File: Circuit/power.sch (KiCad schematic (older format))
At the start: 19 parts, among them Q202 FDN340P, Q203 FDN340P, SW1 ON/OFF, U201 CN3063, U202 MCP6002, U3 LXDC2XQ

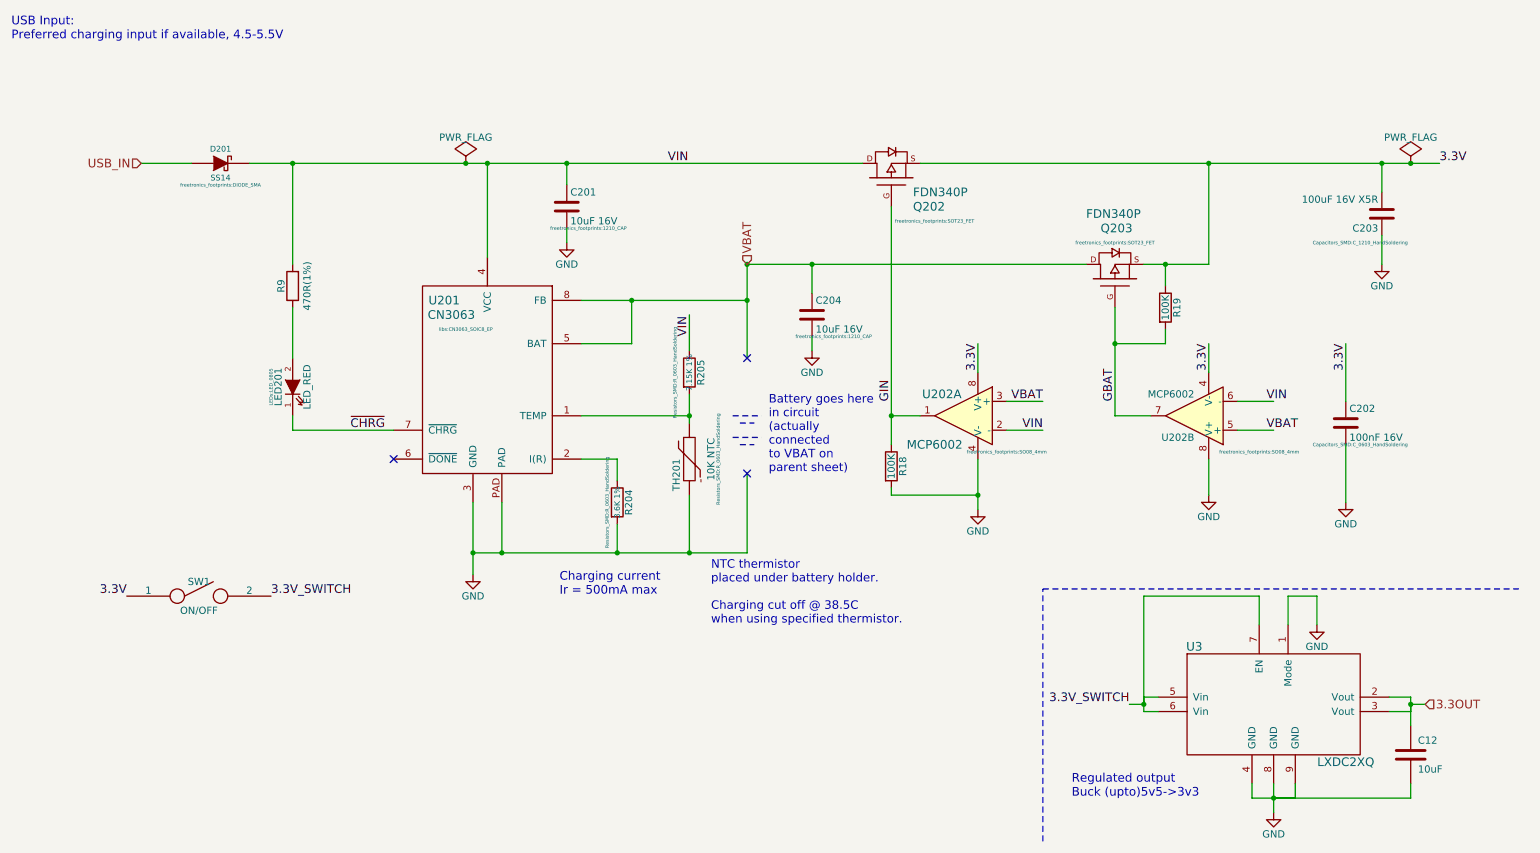
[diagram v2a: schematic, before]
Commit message: BOM information to schematic. Power & main sheets mostly.
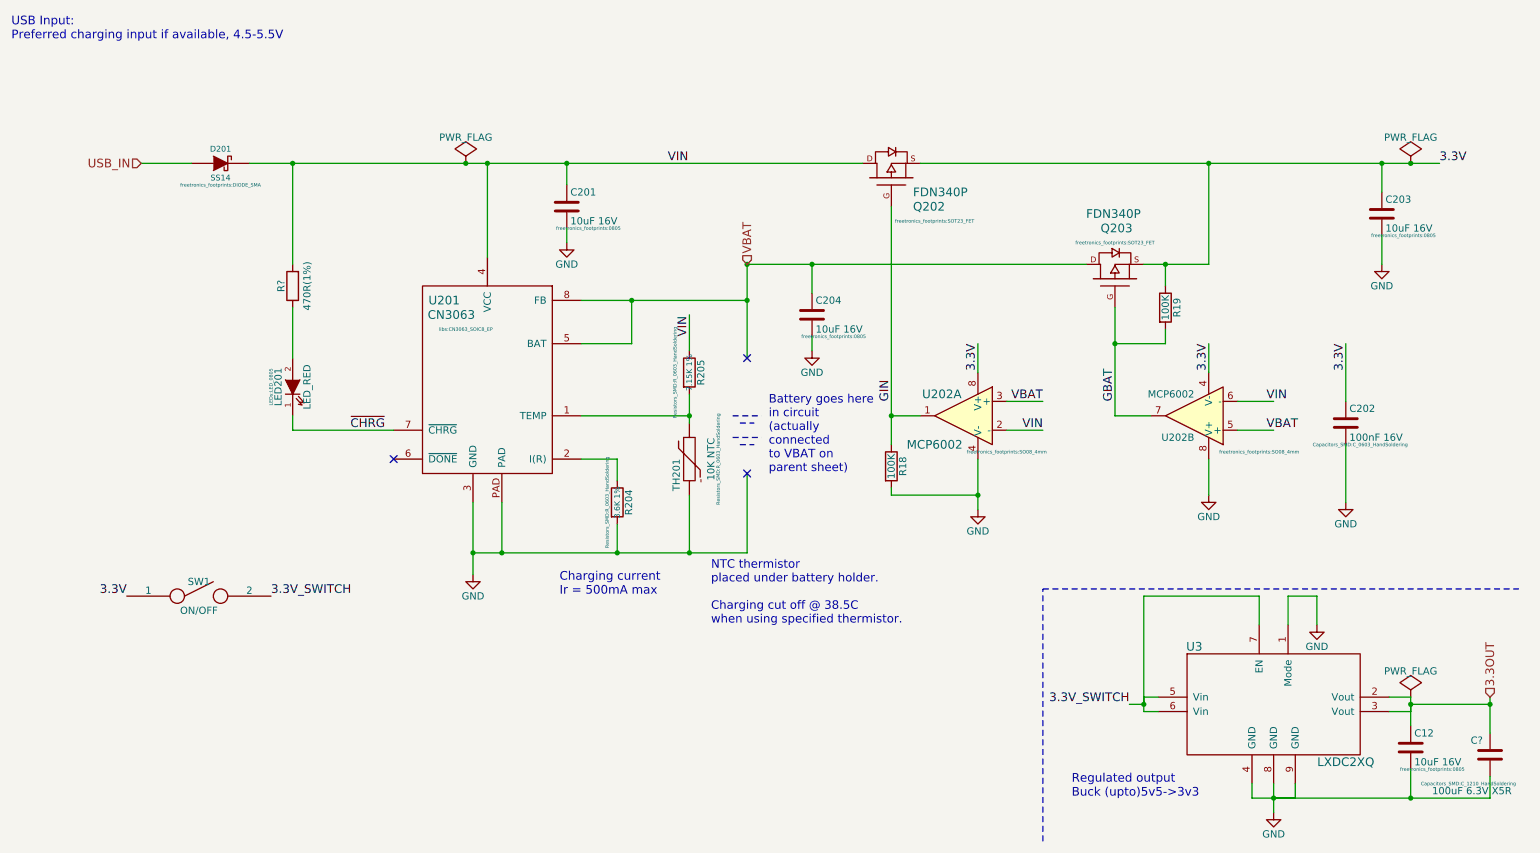
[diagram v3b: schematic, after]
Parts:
- removed C12: 10uF, Capacitors_SMD:C_0603_HandSoldering, symbol CAP
- added C12, C203: 10uF 16V, freetronics_footprints:0805, symbol C
- C201, C204: footprint freetronics_footprints:1210_CAP -> freetronics_footprints:0805; Digikey PN 1276-2865-1-ND -> 1276-2399-1-ND; Link http://www.digikey.com.au/product-detail/en/samsung-electro-mechanics-america-inc/CL32F106ZOHNNNE/1276-2865-1-ND/3890951 -> http://www.digikey.com.au/product-detail/en/samsung-electro-mechanics-america-inc/CL21A106KOCLRNC/1276-2399-1-ND/3890485; Manufacturer PN CL32F106ZOHNNNE -> CL21A106KOCLRNC; Unit Cost 0.29 -> 0.18
- C?: renamed from C203; value 100uF 16V X5R -> 100uF 6.3V X5R; Digikey PN (none) -> 490-7217-1-ND; Link (none) -> http://www.digikey.com.au/product-detail/en/murata-electron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; Manufacturer PN (none) -> GRM31CR60J107ME39K; Unit Cost (none) -> 0.60
- U202: Digikey PN (none) -> MCP6002T-I/SNCT-ND; Link (none) -> http://www.digikey.com.au/product-detail/en/microchip-techn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; Manufacturer PN (none) -> MCP6002T-I/SN; Unit Cost (none) -> 0.33
- renumbered R9 to R?
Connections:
- wire segments 72 -> 74
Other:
- moved on the sheet: C?
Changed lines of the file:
@@
 Text Label 6850 3450 1    60   ~ 0
 GIN
-Text HLabel 10550 5550 2    60   Input ~ 0
+Text HLabel 11000 5500 1    60   Input ~ 0
 3.3OUT
 $Comp
@@
 F 2 "freetronics_footprints:SO08_4mm" H 7050 3300 24  0000 C CNN
 F 3 "" H 7350 3550 60  0000 C CNN
+F 4 "MCP6002T-I/SNCT-ND" H 7350 3550 60  0001 C CNN "Digikey PN"
+F 5 "http://www.digikey.com.au/product-detail/en/microchip-technology/MCP6002T-I-SN/MCP6002T-I-SNCT-ND/4307905" H 7350 3550 60  0001 C CNN "Link"
+F 6 "MCP6002T-I/SN" H 7350 3550 60  0001 C CNN "Manufacturer PN"
+F 7 "0.33" H 7350 3550 60  0001 C CNN "Unit Cost"
 	1    7350 3550
 	-1   0    0    -1
@@
 VIN
 $Comp
-L C C203
+L C C?
 U 1 1 5642CCBE
-P 10250 2150
-F 0 "C203" H 10275 2250 50  0000 L CNN
-F 1 "100uF 16V X5R" H 10275 2050 50  0000 L CNN
-F 2 "Capacitors_SMD:C_1210_HandSoldering" H 10400 2350 24  0000 C CNN
-F 3 "" H 10250 2150 60  0000 C CNN
-	1    10250 2150
+P 11000 5900
+F 0 "C?" H 11050 5800 50  0000 L CNN
+F 1 "100uF 6.3V X5R" H 10850 6150 50  0000 L CNN
+F 2 "Capacitors_SMD:C_1210_HandSoldering" H 11150 6100 24  0000 C CNN
+F 3 "" H 11000 5900 60  0000 C CNN
+F 4 "490-7217-1-ND" H 11000 5900 60  0001 C CNN "Digikey PN"
+F 5 "http://www.digikey.com.au/product-detail/en/murata-electronics-north-america/GRM31CR60J107ME39K/490-7217-1-ND/3991203" H 11000 5900 60  0001 C CNN "Link"
+F 6 "GRM31CR60J107ME39K" H 11000 5900 60  0001 C CNN "Manufacturer PN"
+F 7 "0.60" H 11000 5900 60  0001 C CNN "Unit Cost"
+	1    11000 5900
 	-1   0    0    1
 $EndComp
@@
 F 0 "C201" H 4625 2200 50  0000 L CNN
 F 1 "10uF 16V" H 4625 2000 50  0000 L CNN
-F 2 "freetronics_footprints:1210_CAP" H 4750 1950 24  0000 C CNN
+F 2 "freetronics_footprints:0805" H 4750 1950 24  0000 C CNN
 F 3 "" H 4600 2100 60  0000 C CNN
-F 4 "1276-2865-1-ND" H 4600 2100 60  0001 C CNN "Digikey PN"
-F 5 "http://www.digikey.com.au/product-detail/en/samsung-electro-mechanics-america-inc/CL32F106ZOHNNNE/1276-2865-1-ND/3890951" H 4600 2100 60  0001 C CNN "Link"
-F 6 "CL32F106ZOHNNNE" H 4600 2100 60  0001 C CNN "Manufacturer PN"
-F 7 "0.29" H 4600 2100 60  0001 C CNN "Unit Cost"
+F 4 "1276-2399-1-ND" H 4600 2100 60  0001 C CNN "Digikey PN"
+F 5 "http://www.digikey.com.au/product-detail/en/samsung-electro-mechanics-america-inc/CL21A106KOCLRNC/1276-2399-1-ND/3890485" H 4600 2100 60  0001 C CNN "Link"
+F 6 "CL21A106KOCLRNC" H 4600 2100 60  0001 C CNN "Manufacturer PN"
+F 7 "0.18" H 4600 2100 60  0001 C CNN "Unit Cost"
 	1    4600 2100
 	1    0    0    -1
@@
 	1    0    0    -1
 $EndComp
-$Comp
-L CAP C12
-U 1 1 5812F47A
-P 10450 5900
-F 0 "C12" H 10500 6000 50  0000 L CNN
-F 1 "10uF" H 10500 5800 50  0000 L CNN
-F 2 "Capacitors_SMD:C_0603_HandSoldering" H 10450 5900 60  0001 C CNN
-F 3 "" H 10450 5900 60  0000 C CNN
-	1    10450 5900
-	1    0    0    -1
-$EndComp
 Wire Wire Line
 	5050 3050 5050 2750
@@
 	10450 5500 10450 5600
 Wire Wire Line
-	10450 5550 10550 5550
+	10450 5550 11000 5550
 Wire Wire Line
 	10450 5600 10300 5600
@@
 	10450 5550 10450 5700
 Wire Wire Line
-	10450 6100 10450 6200
-Wire Wire Line
-	10450 6200 9500 6200
+	10450 6000 10450 6200
+Wire Wire Line
+	9500 6200 11000 6200
 $Comp
 L LXDC2XQ U3
@@
 NoConn ~ 5850 3950
 $Comp
-L R R9
+L R R?
 U 1 1 5820F348
 P 2700 2650
-F 0 "R9" V 2780 2650 50  0000 C CNN
+F 0 "R?" V 2780 2650 50  0000 C CNN
 F 1 "470R(1%)" V 2600 2650 50  0000 C CNN
 F 2 "Resistors_SMD:R_0603_HandSoldering" V 2630 2650 50  0001 C CNN
@@
 	-1   0    0    1
 $EndComp
+Wire Wire Line
+	11000 5500 11000 5750
+Connection ~ 11000 5550
+Wire Wire Line
+	11000 6200 11000 6050
+Connection ~ 10450 6200
+$Comp
+L PWR_FLAG #FLG?
+U 1 1 58217320
+P 10450 5500
+F 0 "#FLG?" H 10450 5595 50  0001 C CNN
+F 1 "PWR_FLAG" H 10450 5680 50  0000 C CNN
+F 2 "" H 10450 5500 60  0000 C CNN
+F 3 "" H 10450 5500 60  0000 C CNN
+	1    10450 5500
+	1    0    0    -1
+$EndComp
 $Comp
 L C C204
-U 1 1 5820F69B
+U 1 1 58217FC8
 P 6300 2850
 F 0 "C204" H 6325 2950 50  0000 L CNN
 F 1 "10uF 16V" H 6325 2750 50  0000 L CNN
-F 2 "freetronics_footprints:1210_CAP" H 6450 2700 24  0000 C CNN
+F 2 "freetronics_footprints:0805" H 6450 2700 24  0000 C CNN
 F 3 "" H 6300 2850 60  0000 C CNN
-F 4 "1276-2865-1-ND" H 6300 2850 60  0001 C CNN "Digikey PN"
-F 5 "http://www.digikey.com.au/product-detail/en/samsung-electro-mechanics-america-inc/CL32F106ZOHNNNE/1276-2865-1-ND/3890951" H 6300 2850 60  0001 C CNN "Link"
-F 6 "CL32F106ZOHNNNE" H 6300 2850 60  0001 C CNN "Manufacturer PN"
-F 7 "0.29" H 6300 2850 60  0001 C CNN "Unit Cost"
+F 4 "1276-2399-1-ND" H 6300 2850 60  0001 C CNN "Digikey PN"
+F 5 "http://www.digikey.com.au/product-detail/en/samsung-electro-mechanics-america-inc/CL21A106KOCLRNC/1276-2399-1-ND/3890485" H 6300 2850 60  0001 C CNN "Link"
+F 6 "CL21A106KOCLRNC" H 6300 2850 60  0001 C CNN "Manufacturer PN"
+F 7 "0.18" H 6300 2850 60  0001 C CNN "Unit Cost"
 	1    6300 2850
 	1    0    0    -1
 $EndComp
+$Comp
+L C C203
+U 1 1 582182F8
+P 10250 2150
+F 0 "C203" H 10275 2250 50  0000 L CNN
+F 1 "10uF 16V" H 10275 2050 50  0000 L CNN
+F 2 "freetronics_footprints:0805" H 10400 2000 24  0000 C CNN
+F 3 "" H 10250 2150 60  0000 C CNN
+F 4 "1276-2399-1-ND" H 10250 2150 60  0001 C CNN "Digikey PN"
+F 5 "http://www.digikey.com.au/product-detail/en/samsung-electro-mechanics-america-inc/CL21A106KOCLRNC/1276-2399-1-ND/3890485" H 10250 2150 60  0001 C CNN "Link"
+F 6 "CL21A106KOCLRNC" H 10250 2150 60  0001 C CNN "Manufacturer PN"
+F 7 "0.18" H 10250 2150 60  0001 C CNN "Unit Cost"
+	1    10250 2150
+	1    0    0    -1
+$EndComp
+$Comp
+L C C12
+U 1 1 58218A3F
+P 10450 5850
+F 0 "C12" H 10475 5950 50  0000 L CNN
+F 1 "10uF 16V" H 10475 5750 50  0000 L CNN
+F 2 "freetronics_footprints:0805" H 10600 5700 24  0000 C CNN
+F 3 "" H 10450 5850 60  0000 C CNN
+F 4 "1276-2399-1-ND" H 10450 5850 60  0001 C CNN "Digikey PN"
+F 5 "http://www.digikey.com.au/product-detail/en/samsung-electro-mechanics-america-inc/CL21A106KOCLRNC/1276-2399-1-ND/3890485" H 10450 5850 60  0001 C CNN "Link"
+F 6 "CL21A106KOCLRNC" H 10450 5850 60  0001 C CNN "Manufacturer PN"
+F 7 "0.18" H 10450 5850 60  0001 C CNN "Unit Cost"
+	1    10450 5850
+	1    0    0    -1
+$EndComp
